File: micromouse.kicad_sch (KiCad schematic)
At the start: 15 parts, among them J1 XT60-M, SW1 SW_SPST, SW2 SW_Push, SW3 SW_SPDT_312, SW4 SW_Push, U1 BUCK, U2 STM32 Blackpill, U3 N20 encoder right, U4 N20 encoder left, U5 TB6612FNG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

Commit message: ch
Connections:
- net slide_SW: now also U2.9 (A12)
- no-connect marks 26 -> 25
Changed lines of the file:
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@@
-	)
-	(no_connect
-		(at 90.17 77.47)
 	)
 	(no_connect
@@
 				(hide yes)
 			)
+		)
+	)
+	(global_label "slide_SW"
+		(shape input)
+		(at 90.17 77.47 0)
+		(fields_autoplaced yes)
+		(effects
+			(font
+				(size 1.27 1.27)
+			)
+			(justify left)
+		)
+		(property "Intersheetrefs" "${INTERSHEET_REFS}"
+			(at 101.3194 77.47 0)
+			(effects
+				(font
+					(size 1.27 1.27)
+				)
+				(justify left)
+				(hide yes)
+			)

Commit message: pcb changes!!!!!
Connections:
- net GND: now also U2.19 (GND)
- no-connect marks 25 -> 24
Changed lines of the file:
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@@
-	)
-	(no_connect
-		(at 90.17 52.07)
 	)
 	(no_connect
@@
 			(effects
 				(font
+					(size 1.27 1.27)
+				)
+				(justify left)
+				(hide yes)
+			)
+		)
+	)
+	(global_label "GND"
+		(shape input)
+		(at 90.17 52.07 0)
+		(fields_autoplaced yes)
+		(effects
+			(font
+				(size 1.27 1.27)
+			)
+			(justify left)
+		)
+		(property "Intersheetrefs" "${INTERSHEET_REFS}"
+			(at 97.0257 52.07 0)
+			(effects
+				(font

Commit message: pcb
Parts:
- SW2, SW4: footprint push button:push_button -> push button 1:SW_VS-1213-67-160GF
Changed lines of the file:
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@@
 			)
 		)
-		(property "Footprint" "push button:push_button"
+		(property "Footprint" "push button 1:SW_VS-1213-67-160GF"
 			(at 78.74 116.205 0)
 			(effects
@@
 			)
 		)
-		(property "Footprint" "push button:push_button"
+		(property "Footprint" "push button 1:SW_VS-1213-67-160GF"
 			(at 79.375 104.14 0)
 			(effects

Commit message: pcb
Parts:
- SW1: footprint SPST:JUDCOSPST -> power switch:battery_sw
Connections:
- net 3.3v: now also U5.2 (VCC)
- net 5v: no longer U5.2 (VCC)
- net 7.4v: now also SW1.1 (A); no longer SW1.T (A)
- net 7.4vb: now also SW1.2 (B); no longer SW1.P (B)
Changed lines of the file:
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@@
 		)
 	)
-	(global_label "5v"
+	(global_label "3.3v"
 		(shape input)
 		(at 158.115 76.835 0)
@@
 		)
 		(property "Intersheetrefs" "${INTERSHEET_REFS}"
-			(at 163.2773 76.835 0)
+			(at 165.0916 76.835 0)
 			(effects
 				(font
@@
 			)
 		)
-		(property "Footprint" "SPST:JUDCOSPST"
+		(property "Footprint" "power switch:battery_sw"
 			(at 33.655 81.915 0)
 			(effects
@@
 			)
 		)
-		(pin "T"
+		(pin "2"
 		)
-		(pin "P"
+		(pin "1"
 		)
 		(instances

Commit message: hello world
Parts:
- removed U6: VL53L0X left, VL53L0X:VL53L0X, symbol VL53L0X:VL53L0X
- removed U7: VL53L0X right, VL53L0X:VL53L0X, symbol VL53L0X:VL53L0X
- removed U8: VL53L0X middle, VL53L0X:VL53L0X, symbol VL53L0X:VL53L0X
- added U6, U7, U8: VL6180X, VL6180X:VL6180X, symbol VL53L0X:VL6180x
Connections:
- net 3.3v: now also U6.5 (Vin), U7.5 (Vin), U8.5 (Vin)
- net GND: now also U6.6 (GND), U7.6 (GND), U8.6 (GND)
- net SCL: now also U6.3 (SCL), U7.3 (SCL), U8.3 (SCL)
- net SDA: now also U6.4 (SDA), U7.4 (SDA), U8.4 (SDA)
- net XSHUT 1: now also U7.2 (~{XSHUT})
- net XSHUT 2: now also U8.2 (~{XSHUT})
- net XSHUT 3: now also U6.2 (~{XSHUT})

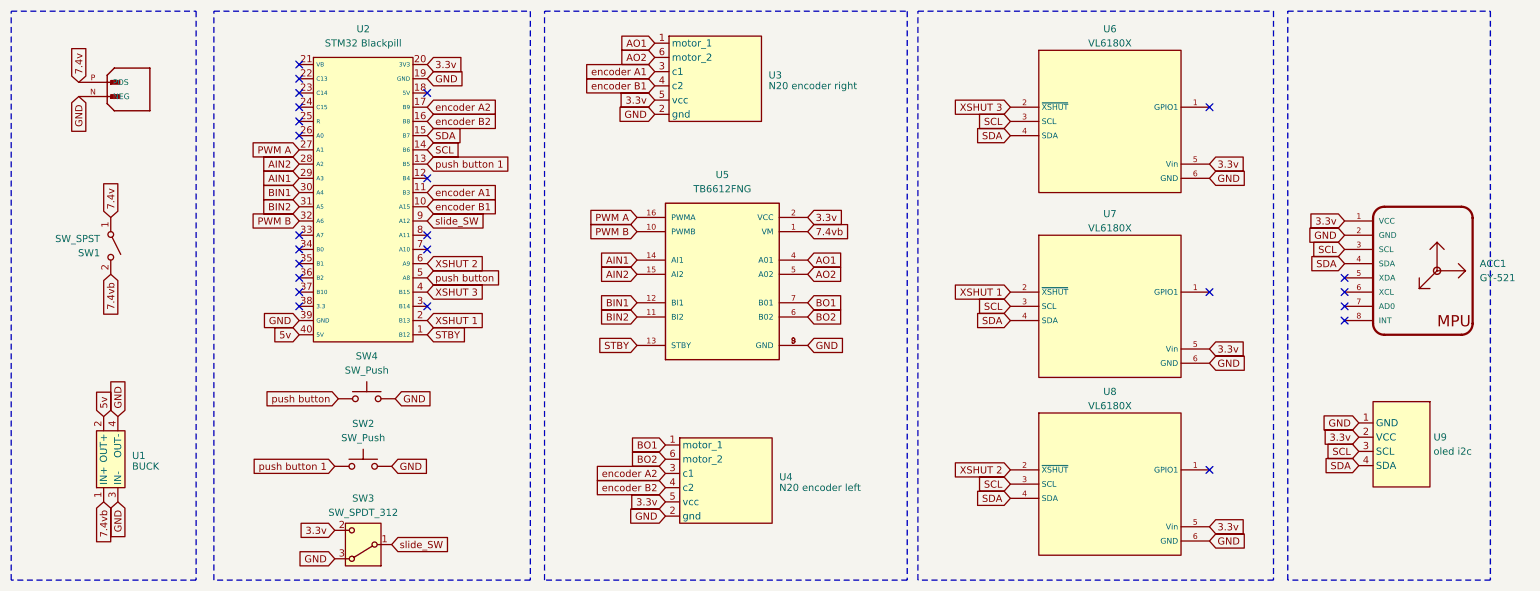
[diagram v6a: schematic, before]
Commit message: added uart
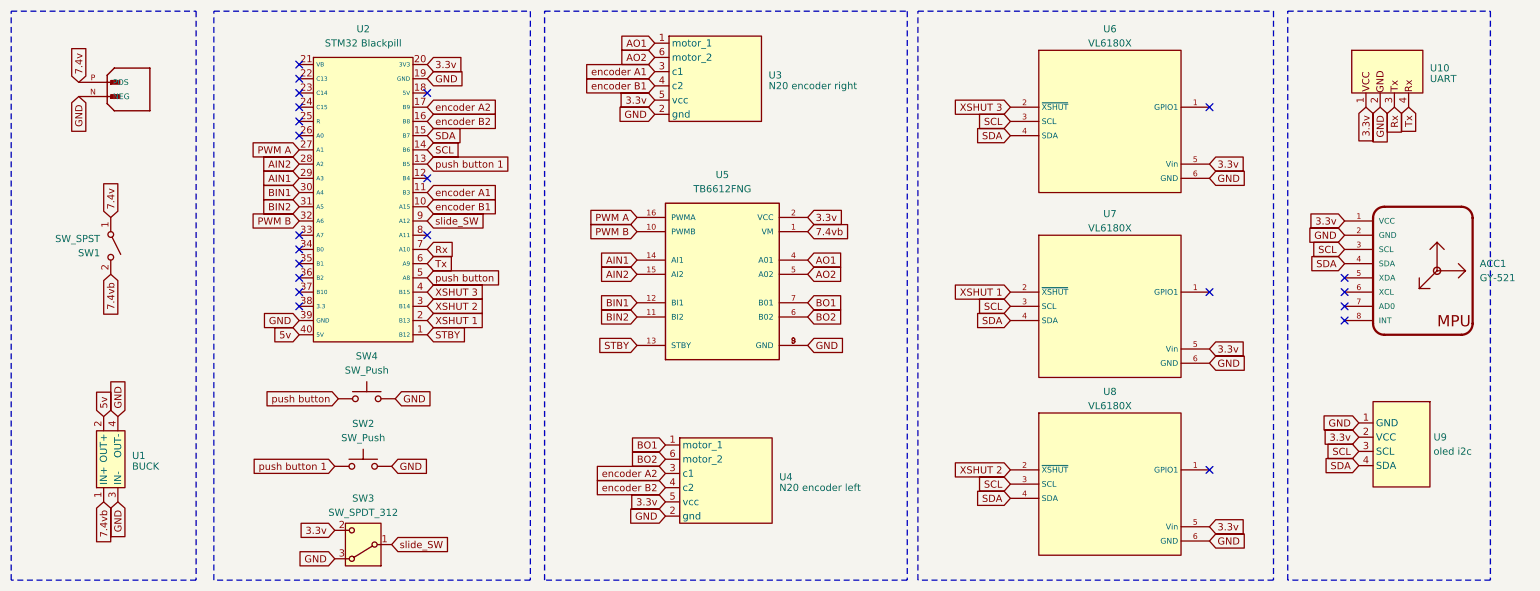
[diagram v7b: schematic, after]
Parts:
- added U10: UART, Connector_PinHeader_2.54mm:PinHeader_1x04_P2.54mm_Vertical, symbol UART:UART
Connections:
- net 3.3v: now also U10.1
- net GND: now also U10.2
- net XSHUT 2: now also U2.3 (B14); no longer U2.6 (A9)
- net Rx: now reaches U2.7 (A10)
- net Rx: now also U10.3
- new net Tx: U10.4, U2.6 (A9)
- no-connect marks 24 -> 22
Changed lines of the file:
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@@
-	)
-	(no_connect
-		(at 90.17 92.71)
 	)
 	(no_connect
@@
 	)
 	(no_connect
-		(at 90.17 82.55)
-	)
-	(no_connect
 		(at 67.31 57.15)
 	)
@@
 		)
 	)
+	(global_label "Rx"
+		(shape input)
+		(at 262.89 57.15 270)
+		(fields_autoplaced yes)
+		(effects
+			(font
+				(size 1.27 1.27)
+			)
+			(justify right)
+		)
+		(property "Intersheetrefs" "${INTERSHEET_REFS}"
+			(at 262.89 62.4333 90)
+			(effects
+				(font
+					(size 1.27 1.27)
+				)
+				(justify right)
+				(hide yes)
+			)
+		)
+	)
 	(global_label "SDA"
 		(shape input)
@@
 		)
 	)
+	(global_label "GND"
+		(shape input)
+		(at 260.35 57.15 270)
+		(fields_autoplaced yes)
+		(effects
+			(font
+				(size 1.27 1.27)
+			)
+			(justify right)
+		)
+		(property "Intersheetrefs" "${INTERSHEET_REFS}"
+			(at 260.35 64.0057 90)
+			(effects
+				(font
+					(size 1.27 1.27)
+				)
+				(justify right)
+				(hide yes)
+			)
+		)
+	)
 	(global_label "BO1"
 		(shape input)
@@
 		)
 	)
+	(global_label "Tx"
+		(shape input)
+		(at 90.17 85.09 0)
+		(fields_autoplaced yes)
+		(effects
+			(font
+				(size 1.27 1.27)
+			)
+			(justify left)
+		)
+		(property "Intersheetrefs" "${INTERSHEET_REFS}"
+			(at 95.1509 85.09 0)
+			(effects
+				(font
+					(size 1.27 1.27)
+				)
+				(justify left)
+				(hide yes)
+			)
+		)
+	)
 	(global_label "GND"
 		(shape input)
@@
 		)
 	)
+	(global_label "Rx"
+		(shape input)
+		(at 90.17 82.55 0)
+		(fields_autoplaced yes)
+		(effects
+			(font
+				(size 1.27 1.27)
+			)
+			(justify left)
+		)
+		(property "Intersheetrefs" "${INTERSHEET_REFS}"
+			(at 95.4533 82.55 0)
+			(effects
+				(font
+					(size 1.27 1.27)
+				)
+				(justify left)
+				(hide yes)
+			)
+		)
+	)
 	(global_label "GND"
 		(shape input)
@@
 		)
 	)
+	(global_label "Tx"
+		(shape input)
+		(at 265.43 57.15 270)
+		(fields_autoplaced yes)
+		(effects
+			(font
+				(size 1.27 1.27)
+			)
+			(justify right)
+		)
+		(property "Intersheetrefs" "${INTERSHEET_REFS}"
+			(at 265.43 62.1309 90)
+			(effects
+				(font
+					(size 1.27 1.27)
+				)
+				(justify right)
+				(hide yes)
+			)
+		)
+	)
 	(global_label "XSHUT 2"
 		(shape input)
@@
 		)
 	)
+	(global_label "3.3v"
+		(shape input)
+		(at 257.81 57.15 270)
+		(fields_autoplaced yes)
+		(effects
+			(font
+				(size 1.27 1.27)
+			)
+			(justify right)
+		)
+		(property "Intersheetrefs" "${INTERSHEET_REFS}"
+			(at 257.81 64.1266 90)
+			(effects
+				(font
+					(size 1.27 1.27)
+				)
+				(justify right)
+				(hide yes)
+			)
+		)
+	)
 	(global_label "push button 1"
 		(shape input)
@@
 	(global_label "XSHUT 2"
 		(shape input)
-		(at 90.17 85.09 0)
-		(fields_autoplaced yes)
-		(effects
-			(font
-				(size 1.27 1.27)
-			)
-			(justify left)
-		)
-		(property "Intersheetrefs" "${INTERSHEET_REFS}"
-			(at 101.3799 85.09 0)
+		(at 90.17 92.71 0)
+		(fields_autoplaced yes)
+		(effects
+			(font
+				(size 1.27 1.27)
+			)
+			(justify left)
+		)
+		(property "Intersheetrefs" "${INTERSHEET_REFS}"
+			(at 101.3799 92.71 0)
 			(effects
 				(font
@@
 					(unit 1)
 				)
+			)
+		)
+	)
+	(symbol
+		(lib_id "UART:UART")
+		(at 261.62 50.8 0)
+		(unit 1)
+		(exclude_from_sim no)
+		(in_bom yes)
+		(on_board yes)
+		(dnp no)
+		(fields_autoplaced yes)
+		(property "Reference" "U10"
+			(at 269.24 50.1649 0)
+			(effects
+				(font
+					(size 1.27 1.27)
+				)
+				(justify left)
+			)
+		)
+		(property "Value" "UART"
+			(at 269.24 52.07 0)
+			(effects
+				(font
+					(size 1.27 1.27)
+				)
+				(justify left)
+			)
+		)
+		(property "Footprint" "Connector_PinHeader_2.54mm:PinHeader_1x04_P2.54mm_Vertical"
+			(at 261.62 50.8 0)
+			(effects
+				(font
+					(size 1.27 1.27)
+				)
+				(hide yes)
+			)
+		)
+		(property "Datasheet" ""
+			(at 261.62 50.8 0)
+			(effects
+				(font
+					(size 1.27 1.27)
+				)
+				(hide yes)
+			)
+		)
+		(property "Description" ""
+			(at 261.62 50.8 0)
+			(effects
+				(font
+					(size 1.27 1.27)
+				)
+				(hide yes)
+			)
+		)
+		(pin "4"
+		)
+		(pin "3"
+		)
+		(pin "2"
+		)
+		(pin "1"
+		)
+		(instances
+			(project ""
+				(path "/ad2eaac4-906f-408a-b5e5-135c4e396716"
+					(reference "U10")
+					(unit 1)
+				)
